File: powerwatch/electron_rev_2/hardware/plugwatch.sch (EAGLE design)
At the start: 110 parts, among them J1 TC2030-JLINK-NL, J2 DM3AT-SF-PEJM5, SW1 SIP3240X, SW2 SIP3240X, SW3 SIP3240X, SW4 SIP3240X, SW7 SIP3240X, U1 MAX-M8, U3 ISL29035, U37 MPU-9250, U4 NRF51822QF, U5 SAFFB1G56KB0F0A, U6 BGA725L6-ALT, U7 OPA322AIDBVT, U8 MAX740XESA, X3 16MHz, X4 ABS05-32.768KHZ-9-T

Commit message: Fix BLE VCC, testpoints, labels, relabel parts
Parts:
- removed A3: ANT3216A063R2400A, chips:ANT3216A063R2400A
- removed C29: 12pF, passives:CAPACITOR0402_CAP
- removed C30: 100nF, passives:CAPACITOR0402_CAP
- removed L6: 15nH, passives:INDUCTOR0402
- removed L7: 10uH, passives:INDUCTOR0603
- removed R26: 100k, passives:RESISTOR0402_RES
- removed SW7: SIP3240X, signpost:SIP3240X
- removed U37: MPU-9250, Testing:MPU-9250
- added ASSY1: ELECTRON, electron:ELECTRON
- added C16, C17: 100nF, passives:CAPACITOR0402_CAP
- added L4, L5: 1k, passives:FERRITE_BEAD0402
- added R22: 100k, passives:RESISTOR0603_RES
- added SW5: SIP3240X, signpost:SIP3240X
- added U2: SAFFB1G56KB0F0A, Particle:FILTERS
- A1: value ELECTRON -> ANT3216A063R2400A; device electron:ELECTRON -> chips:ANT3216A063R2400A; DIGIKEY S7051-ND,S7051-ND -> (none)
- C1: value 100nF -> 0.8pF; DIGIKEY 490-10777-1-ND -> 490-6269-1-ND
- C10: value 2.2uF -> 2.2nF; device passives:CAP_POL1206 -> passives:CAPACITOR0402_CAP; DIGIKEY 718-1131-1-ND -> 490-5419-1-ND
- C12, C13: value 100nF -> 10nF; DIGIKEY 490-10777-1-ND -> 490-7763-1-ND; MPN MF-CAP-0402-0.1uF -> (none); MPN1 GRM155R71A104JA01D -> (none)
- C14: value 100nF -> 47nF; DIGIKEY 490-10777-1-ND -> 490-11420-1-ND; MPN MF-CAP-0402-0.1uF -> (none); MPN1 GRM155R71A104JA01D -> (none)
- C15: value 330pF -> 100nF; DIGIKEY 490-6233-1-ND -> 490-10777-1-ND
- C19: value 1nF -> 100nF; DIGIKEY 490-6366-1-ND -> 490-10777-1-ND
- C2: value 4.7uF -> 4.4pF; device passives:CAPACITOR0402_CAP -> passives:CAPACITOR0603_CAP; DIGIKEY 445-5947-1-ND -> 399-16187-1-ND
- C20: value 4.7uF -> 100nF; DIGIKEY 445-5947-1-ND -> 490-10777-1-ND; MPN (none) -> MF-CAP-0402-0.1uF; MPN1 (none) -> GRM155R71A104JA01D
- C21: value 1uF -> 100nF; DIGIKEY 490-14457-1-ND -> 490-10777-1-ND; MPN (none) -> MF-CAP-0402-0.1uF; MPN1 (none) -> GRM155R71A104JA01D
- C22: value 12pF -> 1uF; DIGIKEY 490-6197-1-ND -> 490-14457-1-ND
- C23: value 12pF -> 2.2uF; device passives:CAPACITOR0402_CAP -> passives:CAP_POL1206; DIGIKEY 490-6197-1-ND -> 718-1131-1-ND
- C24: value 1nF -> 2.2uF; device passives:CAPACITOR0402_CAP -> passives:CAP_POL1206; DIGIKEY 490-6366-1-ND -> 718-1131-1-ND
- C25: value 47nF -> 4.7uF; DIGIKEY 490-11420-1-ND -> 445-5947-1-ND
- C26: value 2.2nF -> 4.7uF; DIGIKEY 490-5419-1-ND -> 445-5947-1-ND
- C27: value 0.8pF -> 10uF; DIGIKEY 490-6269-1-ND -> 490-8316-1-ND
- C28: value 12pF -> 10uF; device passives:CAPACITOR0402_CAP -> passives:CAP_POL1206; DIGIKEY 490-6197-1-ND -> 478-8481-1-ND
- C3, C5: value 10nF -> 12pF; DIGIKEY 490-7763-1-ND -> 490-6197-1-ND
- C4: value 100nF -> 12pF; DIGIKEY 490-10777-1-ND -> 490-6197-1-ND
- C6: value 2.2uF -> 12pF; device passives:CAP_POL1206 -> passives:CAPACITOR0402_CAP; DIGIKEY 718-1131-1-ND -> 490-6197-1-ND
- C7: value 4.4pF -> 330pF; device passives:CAPACITOR0603_CAP -> passives:CAPACITOR0402_CAP; DIGIKEY 399-16187-1-ND -> 490-6233-1-ND
- C8: value 10uF -> 1nF; device passives:CAP_POL1206 -> passives:CAPACITOR0402_CAP; DIGIKEY 478-8481-1-ND -> 490-6366-1-ND
- C9: value 10uF -> 1nF; DIGIKEY 490-8316-1-ND -> 490-6366-1-ND
- J1: value TC2030-JLINK-NL -> DM3AT-SF-PEJM5; device connector:TC2030-JLINK-NL -> connector:DM3AT-SF-PEJM5
- J2: value DM3AT-SF-PEJM5 -> TC2030-JLINK-NL; device connector:DM3AT-SF-PEJM5 -> connector:TC2030-JLINK-NL
- L2: value 1k -> 10uH; device passives:FERRITE_BEAD0402 -> passives:INDUCTOR0603; DIGIKEY 490-4003-1-ND -> 490-4025-1-ND
- L3: value 1k -> 15nH; device passives:FERRITE_BEAD0402 -> passives:INDUCTOR0402; DIGIKEY 490-4003-1-ND -> 587-1521-1-ND
- R1: value 1k -> 49.9; device passives:RESISTOR0402_RES -> passives:RESISTOR0603_RES; DIGIKEY RMCF0402FT1K00CT-ND -> 541-3003-1-ND
- R12: value 12k -> 10k; DIGIKEY RMCF0402FT12K0CT-ND -> RMCF0402FT10K0CT-ND
- R13: value 1k -> 10k; DIGIKEY RMCF0402FT1K00CT-ND -> RMCF0402FT10K0CT-ND
- R14, R8: value 150 -> 10k; DIGIKEY RMCF0402FT150RCT-ND -> RMCF0402FT10K0CT-ND
- R15: value 10k -> 12k; DIGIKEY RMCF0402FT10K0CT-ND -> RMCF0402FT12K0CT-ND
- R16: value 3.48k -> 100k; device passives:RESISTOR0603_RES -> passives:RESISTOR0402_RES; DIGIKEY 541-3.48KHCT-ND -> 1276-3432-1-ND
- R17, R18, R19: device passives:RESISTOR0603_RES -> passives:RESISTOR0402_RES; DIGIKEY 541-2972-1-ND -> 1276-3432-1-ND
- R2: value 10k -> 150; DIGIKEY RMCF0402FT10K0CT-ND -> RMCF0402FT150RCT-ND
- R20: value 49.9 -> 100k; device passives:RESISTOR0603_RES -> passives:RESISTOR0402_RES; DIGIKEY 541-3003-1-ND -> 1276-3432-1-ND
- R21: value 270k -> 100k; device passives:RESISTOR0603_RES -> passives:RESISTOR0402_RES; DIGIKEY 541-270KHCT-ND -> 1276-3432-1-ND
- R23: value 1k -> 100k; device passives:RESISTOR0402_RES -> passives:RESISTOR0603_RES; DIGIKEY RMCF0402FT1K00CT-ND -> 541-2972-1-ND
- R24: device passives:RESISTOR0402_RES -> passives:RESISTOR0603_RES; DIGIKEY 1276-3432-1-ND -> 541-2972-1-ND
- R25: value 100k -> 270k; device passives:RESISTOR0402_RES -> passives:RESISTOR0603_RES; DIGIKEY 1276-3432-1-ND -> 541-270KHCT-ND
- R3: value 100k -> 150; DIGIKEY 1276-3432-1-ND -> RMCF0402FT150RCT-ND
- R4, R5: value 10k -> 1k; DIGIKEY RMCF0402FT10K0CT-ND -> RMCF0402FT1K00CT-ND
- R6: value 100k -> 1k; DIGIKEY 1276-3432-1-ND -> RMCF0402FT1K00CT-ND
- R7: value 100k -> 3.48k; device passives:RESISTOR0402_RES -> passives:RESISTOR0603_RES; DIGIKEY 1276-3432-1-ND -> 541-3.48KHCT-ND
- S1: value PTS645SM43SMTR92 -> B3U-1000P; device switches:PTS645SM43SMTR92 -> switches:B3U-1000P
- S2: value B3U-1000P -> PTS645SM43SMTR92; device switches:B3U-1000P -> switches:PTS645SM43SMTR92
- U1: value MAX-M8 -> BGA725L6-ALT; device u-blox:MAX-M8 -> Particle:BGA725L6-ALT; DIGIKEY 672-1003-1-ND -> BGA725L6E6327FTSA1CT-ND
- U4: value NRF51822QF -> MAX-M8; device chips:NRF51822QF -> u-blox:MAX-M8; DIGIKEY (none) -> 672-1003-1-ND
- U5: value SAFFB1G56KB0F0A -> MAX740XESA; device Particle:FILTERS -> chips:MAX740XESA; ABACUS_TECHNOLOGIES SAFFB1G56KB0F0A -> (none)
- U6: value BGA725L6-ALT -> MPU-9250; device Particle:BGA725L6-ALT -> Testing:MPU-9250; DIGIKEY BGA725L6E6327FTSA1CT-ND -> 1428-1019-1-ND
- U7: value OPA322AIDBVT -> NRF51822QF; device opamps:OPA322AIDBVT -> chips:NRF51822QF
- U8: value MAX740XESA -> OPA322AIDBVT; device chips:MAX740XESA -> opamps:OPA322AIDBVT
- renumbered A4 to ASSY2, B2 to B1, X3 to X2, X4 to X1
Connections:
- net !GPS_RESET: now also ASSY1.D4, U4.!RESET; no longer A1.D4, U1.!RESET
- net !IMU_INT: now also ASSY1.D2, R11.1, U6.INT; no longer A1.D2, R15.1, U37.INT
- net !LIGHT_INT: now also ASSY1.A1, R8.1; no longer A1.A1, R9.1
- net !SAFEMODE: now also ASSY1.A0, R3.2, S2.P$2; no longer A1.A0, R8.2, S1.P$2
- net !SD_CS: now also ASSY1.A2, J1.DATA3-CD/CS_N, R13.1; no longer A1.A2, J2.DATA3-CD/CS_N, R4.1
- net !SD_DETECT: now also ASSY1.D6, J1.A, R16.1; no longer A1.D6, J2.A, R6.1
- net !WIFI_RESET: now also ASSY1.C4; no longer A1.C4
- net -AMP: now also C2.1, C28.CATHODE, R25.2, U8.-IN; no longer C7.1, C8.CATHODE, R21.2, U7.-IN
- net AUDIO_OUT: now also ASSY1.B2, U5.OUT; no longer A1.B2, U8.OUT
- net AUDIO_PWR_EN: now also ASSY1.B4, R21.1, SW3.EN; no longer A1.B4, R25.1, SW2.EN
- net AVDD1: now also C22.1, C8.1, L3.1, U7.AVDD; no longer C19.1, C21.1, L6.1, U4.AVDD
- net A_MIC_OUT: now also C24.ANODE, R24.2, U5.IN; no longer C10.ANODE, R19.2, U8.IN
- net BLE_PWR_EN: now also ASSY1.B5, R20.1, SW5.EN; no longer A1.B5, R24.1, SW4.EN
- net BLE_RXD: now also ASSY1.C3, U7.P17; no longer A1.C3, U4.P17
- net BLE_TXD: now also ASSY1.C2, U7.P16; no longer A1.C2, U4.P16
- net DCC1: now also L2.2, U7.DCC; no longer L7.2, U4.DCC
- net GND: now also ASSY1.GND, ASSY1.GND@2, C10.2, C12.1, C16.2, C17.2, C23.ANODE, C27.1, C4.2, C5.2, C6.2, C7.1, C8.2, C9.2, J1.B, R15.2, R23.1, R24.1, SW5.GND, U1.GND@4, U2.GND, U4.GND@1, U4.GND@10, U4.GND@12, U6.AD0/SDO, U6.FSYNC, U6.GND, U7.GND, U8.V-; no longer A1.GND@2, A3.GND, C12.2, C2.2, C23.2, C24.2, C27.2, C28.2, C29.2, C30.2, C4.1, C5.1, C6.ANODE, C9.1, J2.B, R12.2, R18.1, R19.1, SW7.GND, U1.GND@10, U1.GND@12, U37.AD0/SDO, U37.FSYNC, U37.GND, U4.GND, U6.GND@1, U6.GND@4, U7.V-, U8.GND
- net GPS_PWR_EN: now also ASSY1.D3, R18.1, SW2.EN; no longer A1.D3, R3.1, SW1.EN
- net GPS_RF_IN: now also U2.OUTPUT, U4.RF_IN; no longer U1.RF_IN, U5.OUTPUT
- net GPS_RXD: now also ASSY1.TX, L5.P$2; no longer A1.TX, L3.P$2
- net GPS_TXD: now also ASSY1.RX, L4.P$2; no longer A1.RX, L2.P$2
- net GPS_VCC: now also C12.2, C15.2, C27.2, R4.2, SW2.VLOAD, U4.VCC, U4.VCC_IO, U4.V_BCKP; no longer C11.2, C4.2, C9.2, R1.2, SW1.VLOAD, U1.VCC, U1.VCC_IO, U1.V_BCKP
- net LED: now also ASSY1.C5; no longer A1.C5
- net LNA_IN: now also U1.AI; no longer U6.AI
- net LNA_OUT: now also U1.AO, U2.INPUT; no longer U5.INPUT, U6.AO
- net N$1: now also R4.1; no longer R1.1
- net N$10: now also U7.ANT1; no longer U4.ANT1
- net N$11: now also C21.1, U5.COM, U5.OS; no longer C13.1, U8.COM, U8.OS
- net N$12: now also U7.ANT2; no longer U4.ANT2
- net N$13: now also A1.ANTENNA, C1.1; no longer A3.ANTENNA, C27.1
- net N$14: now also SW4.VLOAD; no longer SW3.VLOAD
- net N$15: now also L2.1, L3.2; no longer L6.2, L7.1
- net N$18: now also C26.1, J1.VCC, R12.2, R13.2, R14.2, R16.2, SW1.VLOAD; no longer C2.1, J2.VCC, R2.2, R4.2, R5.2, R6.2, SW7.VLOAD
- net N$2: now also U4.TIMEPULSE; no longer U1.TIMEPULSE
- net N$20: now also C3.1, U7.XC1; no longer C22.1, U4.XC1
- net N$21: now also C4.1, U7.XC2; no longer C23.1, U4.XC2
- net N$22: now also C9.1, U7.DEC1; no longer C24.1, U4.DEC1
- net N$24: now also C14.1, U7.DEC2; no longer C25.1, U4.DEC2
- net N$25: now also R5.2; no longer R13.2
- net N$26: now also R2.2, S1.P$2; no longer R14.2, S2.P$2
- net N$3: now also R6.2; no longer R23.2
- net N$4: now also C28.ANODE, R7.1; no longer C8.ANODE, R16.1
- net N$40: now also L4.P$1, U4.TXD; no longer L2.P$1, U1.TXD
- net N$41: now also L5.P$1, U4.RXD; no longer L3.P$1, U1.RXD
- net N$5: now also C2.2, R1.2, R25.1, U8.OUT; no longer C7.2, R20.2, R21.1, U7.OUT
- net N$6: now also C7.2, U5.CLK; no longer C15.2, U8.CLK
- net N$7: now also C24.CATHODE, R1.1; no longer C10.CATHODE, R20.1
- net N$9: now also C23.CATHODE, R22.1, R23.2, U8.+IN; no longer C6.CATHODE, R17.1, R18.2, U7.+IN
- net NRF_A2: now also C6.1, U7.P27/AIN1/XL1; no longer C29.1, U4.P27/AIN1/XL1
- net NRF_A3: now also C5.1, U7.P26/AIN0/XL2; no longer C28.1, U4.P26/AIN0/XL2
- net NRF_P29: now also U7.P29; no longer U4.P29
- net NRF_SWDCLK: now also J2.SWDCLK, R15.1, U7.SWDCLK; no longer J1.SWDCLK, R12.1, U4.SWDCLK
- net NRF_SWDIO/!RESET: now also ASSY1.D7, J2.SWDIO, R2.1, U7.SWDIO/!RESET; no longer A1.D7, J1.SWDIO, R14.1, U4.SWDIO/!RESET
- net REGOUT: now also C18.1, U6.REGOUT; no longer C1.1, U37.REGOUT
- net SD_ENABLE_POWER: now also R17.1, SW1.EN; no longer R7.1, SW7.EN
- net SD_MISO: now also ASSY1.A4, J1.DATA0/MISO, R14.1; no longer A1.A4, J2.DATA0/MISO, R5.1
- net SD_MOSI: now also ASSY1.A5, J1.CMD/MOSI, R12.1; no longer A1.A5, J2.CMD/MOSI, R2.1
- net SD_SCLK: now also ASSY1.A3, J1.CLK; no longer A1.A3, J2.CLK
- net SENSORS_SCL: now also ASSY1.D1, R10.1, U6.SCL/SCLK; no longer A1.D1, R11.1, U37.SCL/SCLK
- net SENSORS_SDA: now also ASSY1.D0, R9.1, U6.SDA/SDI; no longer A1.D0, R10.1, U37.SDA/SDI
- net VCC: now also ASSY1.3V3, C13.1, C17.1, C19.1, R17.2, R18.2, R19.2, R20.2, R21.2, R3.1, R6.1, R8.2, SW5.VSUPP, U6.!CS, U6.VDD, U6.VDDIO; no longer A1.3V3, C14.1, C3.1, C30.1, R15.2, R23.1, R24.2, R25.2, R26.2, R3.2, R7.2, R8.1, SW7.VSUPP, U37.!CS, U37.VDD, U37.VDDIO
- net VCC_A_MIC: now also C20.1, R22.2, R7.2, SW3.VLOAD, U5.!SHDN, U5.VDD, U8.V+; no longer C12.1, R16.2, R17.2, SW2.VLOAD, U7.V+, U8.!SHDN, U8.VDD
- net VCC_BLE: now also C16.1, C25.1, J2.VCC, R5.1, SW5.VLOAD, U7.VDD; no longer C18.1, C20.1, J1.VCC, R13.1, SW4.VLOAD, U4.VDD
- net VCC_RF: now also C11.2, U1.PON, U1.VCC, U4.VCC_RF; no longer C5.2, U1.VCC_RF, U6.PON, U6.VCC
- net VDD_PA1: now also C10.1, U7.VDD_PA; no longer C26.1, U4.VDD_PA
- net WIFI_PWR_EN: now also ASSY1.B1, R19.1, SW4.EN; no longer A1.B1, R26.1, SW3.EN
- net WIFI_RXD: now also ASSY1.C1; no longer A1.C1
- net WIFI_TXD: now also ASSY1.C0; no longer A1.C0

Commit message: Fix BOM issues
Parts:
- C17, C20, C21: MPN MF-CAP-0402-0.1uF -> (none); MPN1 GRM155R71A104JA01D -> (none)
- D2, D3: DIGIKEY (none) -> 160-1837-6-ND
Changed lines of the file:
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@@
 <part name="C17" library="passives" deviceset="CAPACITOR" device="0402_CAP" value="100nF">
 <attribute name="DIGIKEY" value="490-10777-1-ND"/>
-<attribute name="MPN" value="MF-CAP-0402-0.1uF"/>
-<attribute name="MPN1" value="GRM155R71A104JA01D"/>
 </part>
 <part name="P+3" library="supply1" deviceset="VCC" device=""/>
@@
 <part name="C20" library="passives" deviceset="CAPACITOR" device="0402_CAP" value="100nF">
 <attribute name="DIGIKEY" value="490-10777-1-ND"/>
-<attribute name="MPN" value="MF-CAP-0402-0.1uF"/>
-<attribute name="MPN1" value="GRM155R71A104JA01D"/>
 </part>
 <part name="C21" library="passives" deviceset="CAPACITOR" device="0402_CAP" value="100nF">
 <attribute name="DIGIKEY" value="490-10777-1-ND"/>
-<attribute name="MPN" value="MF-CAP-0402-0.1uF"/>
-<attribute name="MPN1" value="GRM155R71A104JA01D"/>
 </part>
 <part name="GND19" library="supply1" library_urn="urn:adsk.eagle:library:371" deviceset="GND" device=""/>
@@
 <part name="GND33" library="supply1" library_urn="urn:adsk.eagle:library:371" deviceset="GND" device=""/>
 <part name="P+13" library="supply1" library_urn="urn:adsk.eagle:library:371" deviceset="VCC" device=""/>
-<part name="D2" library="leds" deviceset="LED" device="0603"/>
+<part name="D2" library="leds" deviceset="LED" device="0603">
+<attribute name="DIGIKEY" value="160-1837-6-ND"/>
+</part>
 <part name="R6" library="passives" deviceset="RESISTOR" device="0402_RES" value="1k">
 <attribute name="DIGIKEY" value="RMCF0402FT1K00CT-ND"/>
 </part>
 <part name="P+14" library="supply1" library_urn="urn:adsk.eagle:library:371" deviceset="VCC" device=""/>
-<part name="D3" library="leds" deviceset="LED" device="0603"/>
+<part name="D3" library="leds" deviceset="LED" device="0603">
+<attribute name="DIGIKEY" value="160-1837-6-ND"/>
+</part>
 <part name="SW2" library="signpost" deviceset="SIP3240X" device=""/>
 <part name="SW3" library="signpost" deviceset="SIP3240X" device=""/>
@@
 </instance>
 <instance part="P+14" gate="VCC" x="17.78" y="132.08"/>
-<instance part="D3" gate="G$1" x="17.78" y="111.76" rot="R270"/>
+<instance part="D3" gate="G$1" x="17.78" y="111.76" rot="R270">
+<attribute name="DIGIKEY" x="17.78" y="111.76" size="1.778" layer="96" rot="R270" display="off"/>
+</instance>
 <instance part="TP1" gate="G$1" x="215.9" y="129.54" rot="R180"/>
 <instance part="TP2" gate="G$1" x="215.9" y="127" rot="R180"/>
@@
 <instance part="A1" gate="G$1" x="180.34" y="86.36"/>
 <instance part="GND2" gate="1" x="185.42" y="40.64"/>
-<instance part="D2" gate="G$1" x="33.02" y="99.06" rot="R270"/>
+<instance part="D2" gate="G$1" x="33.02" y="99.06" rot="R270">
+<attribute name="DIGIKEY" x="33.02" y="99.06" size="1.778" layer="96" rot="R270" display="off"/>
+</instance>
 <instance part="P+16" gate="VCC" x="187.96" y="185.42"/>
 <instance part="SW5" gate="G$1" x="160.02" y="172.72" rot="R180"/>
@@
 <instance part="C17" gate="G$1" x="10.16" y="45.72">
 <attribute name="DIGIKEY" x="10.16" y="45.72" size="1.778" layer="96" display="off"/>
-<attribute name="MPN1" x="10.16" y="45.72" size="1.778" layer="96" display="off"/>
-<attribute name="MPN" x="10.16" y="45.72" size="1.778" layer="96" display="off"/>
 </instance>
 <instance part="P+3" gate="VCC" x="10.16" y="60.96"/>
@@
 <instance part="C20" gate="G$1" x="167.64" y="149.86">
 <attribute name="DIGIKEY" x="167.64" y="149.86" size="1.778" layer="96" display="off"/>
-<attribute name="MPN1" x="167.64" y="149.86" size="1.778" layer="96" display="off"/>
-<attribute name="MPN" x="167.64" y="149.86" size="1.778" layer="96" display="off"/>
 </instance>
 <instance part="C21" gate="G$1" x="162.56" y="119.38">
 <attribute name="DIGIKEY" x="162.56" y="119.38" size="1.778" layer="96" display="off"/>
-<attribute name="MPN1" x="162.56" y="119.38" size="1.778" layer="96" display="off"/>
-<attribute name="MPN" x="162.56" y="119.38" size="1.778" layer="96" display="off"/>
 </instance>
 <instance part="GND19" gate="1" x="162.56" y="109.22"/>

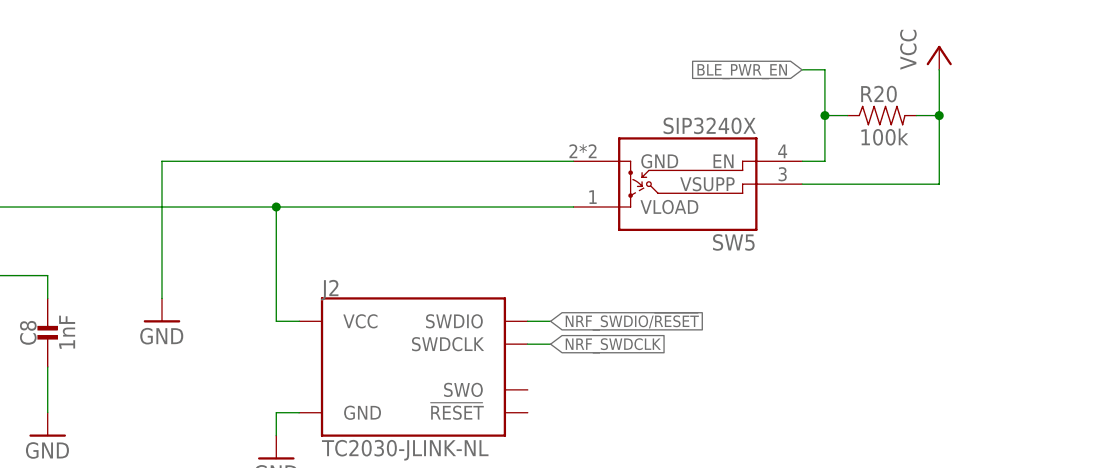
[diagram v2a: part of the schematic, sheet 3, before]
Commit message: add the fixed power switch
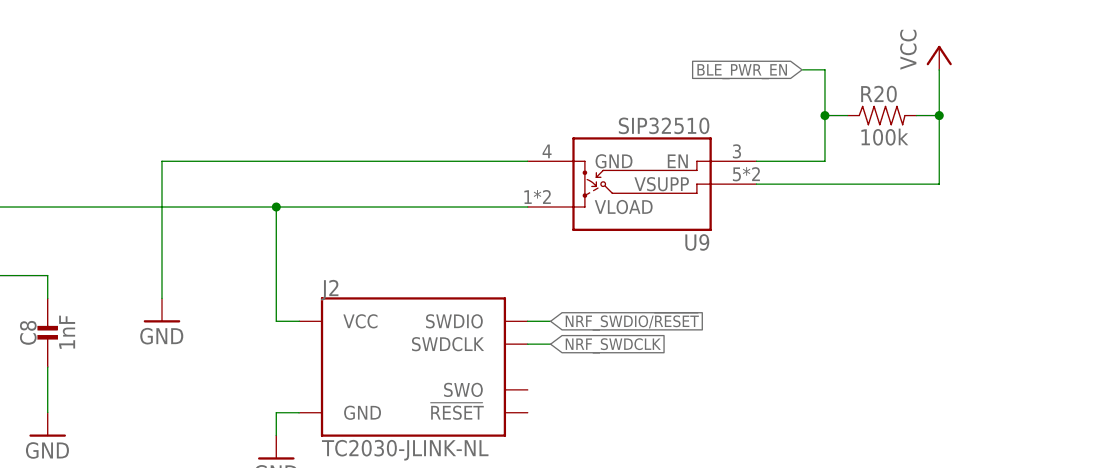
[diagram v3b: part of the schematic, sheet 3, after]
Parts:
- removed SW1, SW2, SW3, SW5: SIP3240X, signpost:SIP3240X
- added U$5, U10, U11, U9: SIP32510, chips:SIP32510
- SW4: value SIP3240X -> SIP32510; device signpost:SIP3240X -> chips:SIP32510
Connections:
- net AUDIO_PWR_EN: now also U11.EN; no longer SW3.EN
- net BLE_PWR_EN: now also U9.EN; no longer SW5.EN
- net GND: now also U$5.GND, U10.GND, U11.GND, U9.GND; no longer SW1.GND, SW2.GND, SW3.GND, SW5.GND
- net GPS_PWR_EN: now also U$5.EN; no longer SW2.EN
- net GPS_VCC: now also U$5.VLOAD; no longer SW2.VLOAD
- net N$18: now also U10.VLOAD; no longer SW1.VLOAD
- net SD_ENABLE_POWER: now also U10.EN; no longer SW1.EN
- net VCC: now also U$5.VSUPP, U10.VSUPP, U11.VSUPP, U9.VSUPP; no longer SW1.VSUPP, SW2.VSUPP, SW3.VSUPP, SW5.VSUPP
- net VCC_A_MIC: now also U11.VLOAD; no longer SW3.VLOAD
- net VCC_BLE: now also U9.VLOAD; no longer SW5.VLOAD
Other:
- moved on the sheet: SW4

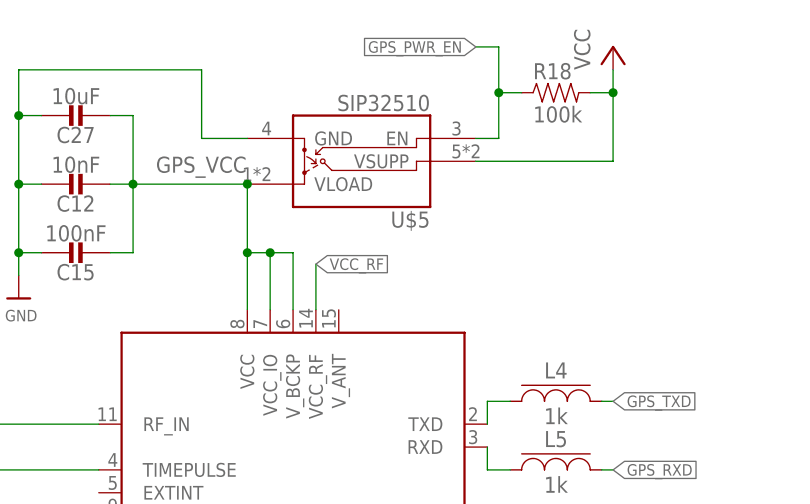
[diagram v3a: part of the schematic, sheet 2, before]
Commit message: fix up silkscreen
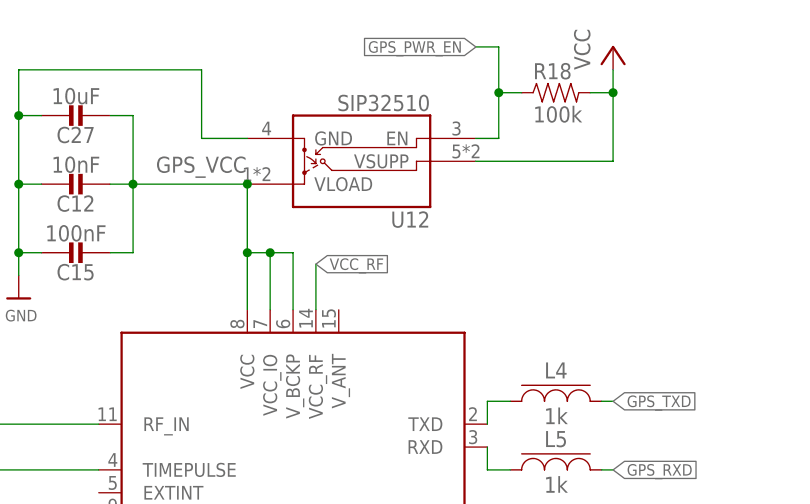
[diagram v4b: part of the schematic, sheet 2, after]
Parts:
- renumbered U$5 to U12
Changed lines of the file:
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@@
 <part name="TP24" library="headers" deviceset="TEST_POINT_0.040IN" device=""/>
 <part name="TP25" library="headers" deviceset="TEST_POINT_0.040IN" device=""/>
-<part name="U$5" library="chips" deviceset="SIP32510" device=""/>
+<part name="U12" library="chips" deviceset="SIP32510" device=""/>
 <part name="U9" library="chips" deviceset="SIP32510" device=""/>
 <part name="U10" library="chips" deviceset="SIP32510" device=""/>
@@
 <attribute name="DIGIKEY" x="114.3" y="71.12" size="1.27" layer="96" font="vector" display="off"/>
 </instance>
-<instance part="U$5" gate="G$1" x="154.94" y="172.72" rot="R180"/>
+<instance part="U12" gate="G$1" x="154.94" y="172.72" rot="R180"/>
 </instances>
 <busses>
@@
 <wire x1="109.22" y1="175.26" x2="109.22" y2="170.18" width="0.1524" layer="91"/>
 <junction x="109.22" y="170.18"/>
-<pinref part="U$5" gate="G$1" pin="GND"/>
+<pinref part="U12" gate="G$1" pin="GND"/>
 </segment>
 <segment>
@@
 <wire x1="160.02" y1="167.64" x2="162.56" y2="167.64" width="0.1524" layer="91"/>
 <junction x="162.56" y="172.72"/>
-<pinref part="U$5" gate="G$1" pin="EN"/>
+<pinref part="U12" gate="G$1" pin="EN"/>
 </segment>
 </net>
@@
 <wire x1="139.7" y1="154.94" x2="137.16" y2="154.94" width="0.1524" layer="91"/>
 <junction x="137.16" y="154.94"/>
-<pinref part="U$5" gate="G$1" pin="VLOAD"/>
+<pinref part="U12" gate="G$1" pin="VLOAD"/>
 <junction x="134.62" y="162.56"/>
 </segment>
@@
 <wire x1="172.72" y1="172.72" x2="175.26" y2="172.72" width="0.1524" layer="91"/>
 <junction x="175.26" y="172.72"/>
-<pinref part="U$5" gate="G$1" pin="VSUPP"/>
-</segment>
-<segment>
+<pinref part="U12" gate="G$1" pin="VSUPP"/>
+</segment>
+<segment>
